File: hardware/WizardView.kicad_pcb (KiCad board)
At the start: 2 copper layers, 4 parts, among them J1 PWR_IN

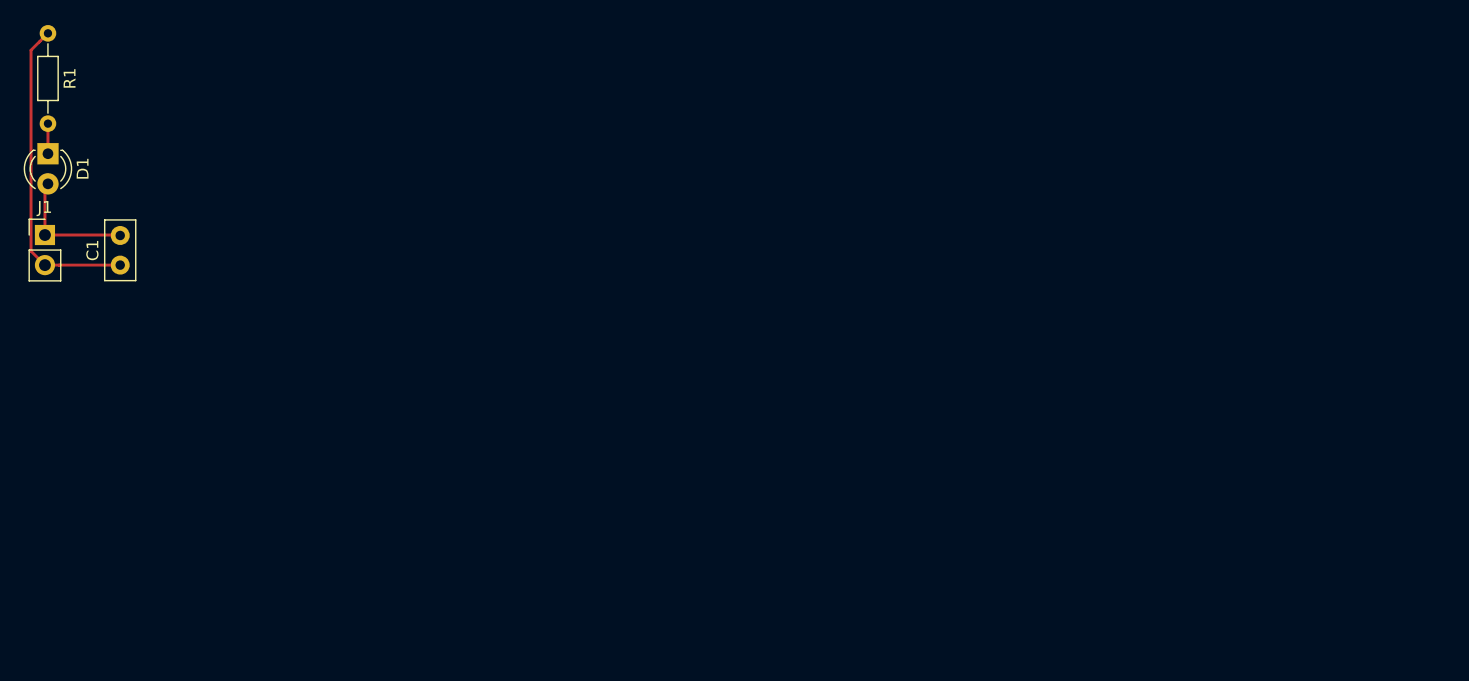
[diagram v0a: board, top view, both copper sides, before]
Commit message: Update KiCad PCB to latest revision.
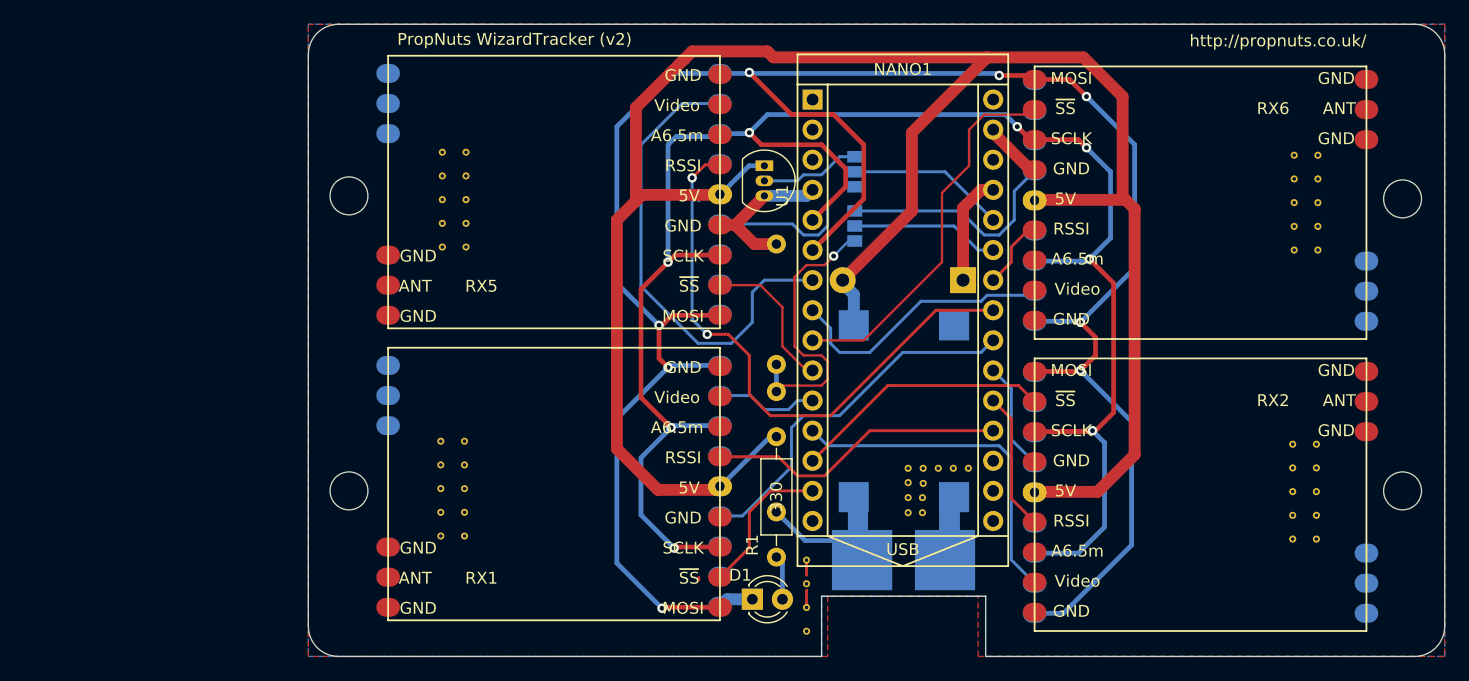
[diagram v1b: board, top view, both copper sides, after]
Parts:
- removed C1: 1uF, Capacitors_THT:C_Disc_D5.0mm_W2.5mm_P2.50mm
- added ?: , Mounting_Holes:MountingHole_3.2mm_M3, F.Cu at (118.4, 91.9)
- added ?: , Mounting_Holes:MountingHole_3.2mm_M3, F.Cu at (118.4, 116.8)
- added ?: , Mounting_Holes:MountingHole_3.2mm_M3, F.Cu at (207.3, 116.8)
- added ?: , Mounting_Holes:MountingHole_3.2mm_M3, F.Cu at (207.3, 92.2)
- added D2: D_Schottky, Diodes_THT:D_DO-41_SOD81_P10.16mm_Horizontal, B.Cu at (170.2, 99.1)
- added G***: LOGO, RX5808:LOGO, B.Cu at (188.7, 91.9)
- added J2: GS3, Connectors:GS3, B.Cu at (161.0, 94.5)
- added J3: GS3, Connectors:GS3, B.Cu at (161.0, 89.9)
- added NANO1: ArduinoNano, RX5808:ArduinoNano, F.Cu at (156.2, 80.0)
- added R2: 100k, Resistors_THT:R_Axial_DIN0207_L6.3mm_D2.5mm_P10.16mm_Horizontal, B.Cu at (154.4, 118.6)
- added R3: 10k, Resistors_THT:R_Axial_DIN0207_L6.3mm_D2.5mm_P10.16mm_Horizontal, B.Cu at (154.4, 106.2)
- added REF**: VIA_STITCH, RX5808:VIA_STITCH, F.Cu at (157.0, 122.7)
- added REF**: VIA_STITCH, RX5808:VIA_STITCH, F.Cu at (168.1, 114.9)
- added REF**: VIA_STITCH, RX5808:VIA_STITCH, F.Cu at (166.8, 114.9)
- added REF**: VIA_STITCH, RX5808:VIA_STITCH, F.Cu at (165.5, 114.9)
- added REF**: VIA_STITCH, RX5808:VIA_STITCH, F.Cu at (165.5, 116.1)
- added REF**: VIA_STITCH, RX5808:VIA_STITCH, F.Cu at (165.5, 117.4)
- added REF**: VIA_STITCH, RX5808:VIA_STITCH, F.Cu at (165.5, 118.7)
- added REF**: VIA_STITCH, RX5808:VIA_STITCH, F.Cu at (200.0, 120.9)
- added REF**: VIA_STITCH, RX5808:VIA_STITCH, F.Cu at (198.0, 120.9)
- added REF**: VIA_STITCH, RX5808:VIA_STITCH, F.Cu at (200.0, 118.9)
- added REF**: VIA_STITCH, RX5808:VIA_STITCH, F.Cu at (198.0, 118.9)
- added REF**: VIA_STITCH, RX5808:VIA_STITCH, F.Cu at (157.0, 128.7)
- added REF**: VIA_STITCH, RX5808:VIA_STITCH, F.Cu at (200.0, 116.9)
- added REF**: VIA_STITCH, RX5808:VIA_STITCH, F.Cu at (198.0, 116.9)
- added REF**: VIA_STITCH, RX5808:VIA_STITCH, F.Cu at (200.0, 114.9)
- added REF**: VIA_STITCH, RX5808:VIA_STITCH, F.Cu at (198.0, 114.9)
- added REF**: VIA_STITCH, RX5808:VIA_STITCH, F.Cu at (200.0, 112.9)
- added REF**: VIA_STITCH, RX5808:VIA_STITCH, F.Cu at (198.0, 112.9)
- added REF**: VIA_STITCH, RX5808:VIA_STITCH, F.Cu at (198.1, 96.5)
- added REF**: VIA_STITCH, RX5808:VIA_STITCH, F.Cu at (200.1, 96.5)
- added REF**: VIA_STITCH, RX5808:VIA_STITCH, F.Cu at (200.1, 94.5)
- added REF**: VIA_STITCH, RX5808:VIA_STITCH, F.Cu at (198.1, 94.5)
- added REF**: VIA_STITCH, RX5808:VIA_STITCH, F.Cu at (157.0, 126.7)
- added REF**: VIA_STITCH, RX5808:VIA_STITCH, F.Cu at (200.1, 92.5)
- added REF**: VIA_STITCH, RX5808:VIA_STITCH, F.Cu at (198.1, 92.5)
- added REF**: VIA_STITCH, RX5808:VIA_STITCH, F.Cu at (200.1, 90.5)
- added REF**: VIA_STITCH, RX5808:VIA_STITCH, F.Cu at (198.1, 90.5)
- added REF**: VIA_STITCH, RX5808:VIA_STITCH, F.Cu at (200.1, 88.5)
- added REF**: VIA_STITCH, RX5808:VIA_STITCH, F.Cu at (198.1, 88.5)
- added REF**: VIA_STITCH, RX5808:VIA_STITCH, F.Cu at (128.2, 96.3)
- added REF**: VIA_STITCH, RX5808:VIA_STITCH, F.Cu at (126.2, 96.3)
- added REF**: VIA_STITCH, RX5808:VIA_STITCH, F.Cu at (128.2, 94.3)
- added REF**: VIA_STITCH, RX5808:VIA_STITCH, F.Cu at (126.2, 94.3)
- added REF**: VIA_STITCH, RX5808:VIA_STITCH, F.Cu at (157.0, 124.7)
- added REF**: VIA_STITCH, RX5808:VIA_STITCH, F.Cu at (128.2, 92.3)
- added REF**: VIA_STITCH, RX5808:VIA_STITCH, F.Cu at (126.2, 92.3)
- added REF**: VIA_STITCH, RX5808:VIA_STITCH, F.Cu at (128.2, 90.3)
- added REF**: VIA_STITCH, RX5808:VIA_STITCH, F.Cu at (126.2, 90.3)
- added REF**: VIA_STITCH, RX5808:VIA_STITCH, F.Cu at (128.2, 88.3)
- added REF**: VIA_STITCH, RX5808:VIA_STITCH, F.Cu at (126.2, 88.3)
- added REF**: VIA_STITCH, RX5808:VIA_STITCH, F.Cu at (128.1, 120.6)
- added REF**: VIA_STITCH, RX5808:VIA_STITCH, F.Cu at (128.1, 118.6)
- added REF**: VIA_STITCH, RX5808:VIA_STITCH, F.Cu at (128.1, 116.6)
- added REF**: VIA_STITCH, RX5808:VIA_STITCH, F.Cu at (128.1, 114.6)
- added REF**: VIA_STITCH, RX5808:VIA_STITCH, F.Cu at (166.8, 118.7)
- added REF**: VIA_STITCH, RX5808:VIA_STITCH, F.Cu at (128.1, 112.6)
- added REF**: VIA_STITCH, RX5808:VIA_STITCH, F.Cu at (126.1, 120.6)
- added REF**: VIA_STITCH, RX5808:VIA_STITCH, F.Cu at (126.1, 118.6)
- added REF**: VIA_STITCH, RX5808:VIA_STITCH, F.Cu at (126.1, 116.6)
- added REF**: VIA_STITCH, RX5808:VIA_STITCH, F.Cu at (126.1, 114.6)
- added REF**: VIA_STITCH, RX5808:VIA_STITCH, F.Cu at (126.1, 112.6)
- added REF**: VIA_STITCH, RX5808:VIA_STITCH, F.Cu at (166.8, 117.4)
- added REF**: VIA_STITCH, RX5808:VIA_STITCH, F.Cu at (166.8, 116.2)
- added REF**: VIA_STITCH, RX5808:VIA_STITCH, F.Cu at (170.6, 114.9)
- added REF**: VIA_STITCH, RX5808:VIA_STITCH, F.Cu at (169.4, 114.9)
- added REF***: OSHW-Logo_11.4x12mm_SilkScreen, Symbols:OSHW-Logo_11.4x12mm_SilkScreen, B.Cu at (136.7, 91.9)
- added REG1: 5VRegulator, RX5808:5VBEC, B.Cu at (170.7, 101.6)
- added RX1: RX5808, RX5808:RX5808, F.Cu at (121.7, 127.8)
- added RX2: RX5808, RX5808:RX5808, F.Cu at (204.2, 105.7)
- added RX3: RX5808, RX5808:RX5808, B.Cu at (204.2, 128.3)
- added RX4: RX5808, RX5808:RX5808, B.Cu at (121.7, 105.2)
- added RX5: RX5808, RX5808:RX5808, F.Cu at (121.7, 103.1)
- added RX6: RX5808, RX5808:RX5808, F.Cu at (204.2, 81.0)
- added RX7: RX5808, RX5808:RX5808, B.Cu at (204.2, 103.6)
- added RX8: RX5808, RX5808:RX5808, B.Cu at (121.7, 80.5)
- added U1: LM35-LP, TO_SOT_Packages_THT:TO-92_Inline_Narrow_Oval, F.Cu at (153.4, 89.4)
- J1: value PWR_IN -> CONN_01X02; footprint Pin_Headers:Pin_Header_Straight_1x02_Pitch2.54mm -> RX5808:XT60_5V; moved to B.Cu
- R1: footprint Resistors_THT:R_Axial_DIN0204_L3.6mm_D1.6mm_P7.62mm_Horizontal -> Resistors_THT:R_Axial_DIN0207_L6.3mm_D2.5mm_P10.16mm_Horizontal
- moved J1 84.0 mm to (171.2, 125.2), turned to 180 degrees
- moved D1 70.3 mm to (152.4, 126.0), turned to 0 degrees
- moved R1 70.3 mm to (154.4, 112.3)
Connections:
- D1 pad 1: Net-(D1-Pad1) -> GND
- D1 pad 2: GND -> Net-(D1-Pad2)
- J1 pad 2: +5V -> +BATT
- R1 pad 2: Net-(D1-Pad1) -> Net-(D1-Pad2)
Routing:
- net /MOSI: track 0.00 -> 189.2 mm, vias 0 -> 8
- net /SCLK: track 0.00 -> 159.5 mm, vias 0 -> 8
- net +5V: track 27.0 -> 178.3 mm
- net /RSSI5: track 0.00 -> 49.1 mm, vias 0 -> 2
- net /~SS8: track 0.00 -> 40.2 mm
- net /~SS6: track 0.00 -> 32.0 mm
- net /RSSI4: track 0.00 -> 31.1 mm
- net /~SS3: track 0.00 -> 29.1 mm
- net /RSSI1: track 0.00 -> 25.3 mm
- net GND: track 10.8 -> 35.7 mm
- net /BATTDIV: track 0.00 -> 24.1 mm, vias 0 -> 1
- net /~SS7: track 0.00 -> 23.6 mm
- net /~SS2: track 0.00 -> 21.9 mm
- net +BATT: track 0.00 -> 20.3 mm
- net /RSSI7: track 0.00 -> 19.7 mm
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- added copper zone on B.Cu, net GND
- added copper zone on F.Cu, net GND
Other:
- board outline added: 95.9 x 53.3 mm
- board text added: "PropNuts WizardTracker (v2)"
- board text added: "http://propnuts.co.uk/"
